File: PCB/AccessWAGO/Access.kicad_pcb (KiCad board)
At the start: 2 copper layers, 70 x 70 mm, 82 parts, among them J1 USB-C, J2 NFC, J3 I/O, J4 TC2030-USB-NL-DS, J5 NFC, J6 GND, J7 12V, J8 DOOR, J9 I/O, Q2 PMF250XNEX, SW1 ESE13V01A, U1 MD8942, U10 ESP32-S3-MINI-1, U2 MD8942, U8 G3VM-41GR8

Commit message: Silkscreen, and 21
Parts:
- added J10: Reset, RevK:AA-Pad, B.Cu at (100.0, 100.0)
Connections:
- U10 pad 25: unconnected-(U10-GPIO21-Pad25) -> Net-(J10-Pin_2)
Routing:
- net Net-(J10-Pin_2): track 0.00 -> 10.5 mm, vias 0 -> 1
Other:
- board text added: "QRQR"
- board text added: "Relay"
- board text added: "®"
- board text removed: "Relay1"

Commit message: Tweak
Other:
- copper layers 2 -> 4
- board text removed: "QRQR"

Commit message: Render
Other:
- copper layers 4 -> 2
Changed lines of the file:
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@@
 		(0 "F.Cu" signal)
 		(2 "B.Cu" signal)
-		(9 "F.Adhes" user)
-		(11 "B.Adhes" user)
+		(9 "F.Adhes" user "F.Adhesive")
+		(11 "B.Adhes" user "B.Adhesive")
 		(13 "F.Paste" user)
 		(15 "B.Paste" user)
-		(5 "F.SilkS" user)
-		(7 "B.SilkS" user)
+		(5 "F.SilkS" user "F.Silkscreen")
+		(7 "B.SilkS" user "B.Silkscreen")
 		(1 "F.Mask" user)
 		(3 "B.Mask" user)
-		(17 "Dwgs.User" user)
-		(19 "Cmts.User" user)
-		(21 "Eco1.User" user)
-		(23 "Eco2.User" user)
+		(17 "Dwgs.User" user "User.Drawings")
+		(19 "Cmts.User" user "User.Comments")
+		(21 "Eco1.User" user "User.Eco1")
+		(23 "Eco2.User" user "User.Eco2")
 		(25 "Edge.Cuts" user)
 		(27 "Margin" user)
-		(31 "F.CrtYd" user)
-		(29 "B.CrtYd" user)
+		(31 "F.CrtYd" user "F.Courtyard")
+		(29 "B.CrtYd" user "B.Courtyard")
 		(35 "F.Fab" user)
 		(33 "B.Fab" user)
-		(39 "User.1" signal)
-		(41 "User.2" signal)
+		(39 "User.1" auxiliary)
+		(41 "User.2" auxiliary "Board outline")
 	)
 	(setup
@@
 	)
 	(gr_arc
-		(start 90.3 108.7)
-		(mid 90.592893 107.992893)
-		(end 91.3 107.7)
-		(stroke
-			(width 0.05)
-			(type default)
-		)
-		(layer "Edge.Cuts")
-	)
-	(gr_arc
-		(start 73.5 108.2)
-		(mid 72.792893 107.907107)
-		(end 72.5 107.2)
+		(start 73.5 108)
+		(mid 72.792893 107.707107)
+		(end 72.5 107)
 		(stroke
 			(width 0.05)
@@
 	)
 	(gr_line
-		(start 72.5 107.2)
+		(start 72.5 107)
 		(end 72.5 77.5)
 		(stroke
@@
 	)
 	(gr_arc
-		(start 132.5 107)
-		(mid 132.207107 107.707107)
-		(end 131.5 108)
+		(start 90.3 108)
+		(mid 90.387868 107.787868)
+		(end 90.6 107.7)
 		(stroke
 			(width 0.05)
@@
 	)
 	(gr_arc
-		(start 108.7 107.7)
-		(mid 109.407107 107.992893)
-		(end 109.7 108.7)
+		(start 109.4 107.7)
+		(mid 109.612132 107.787868)
+		(end 109.7 108)
 		(stroke
 			(width 0.05)
@@
 	)
 	(gr_arc
-		(start 73.5 108.2)
-		(mid 74.5 109.2)
-		(end 73.5 110.2)
+		(start 132.5 107)
+		(mid 132.207107 107.707107)
+		(end 131.5 108)
+		(stroke
+			(width 0.05)
+			(type default)
+		)
+		(layer "Edge.Cuts")
+	)
+	(gr_arc
+		(start 73.5 108)
+		(mid 74.5 109)
+		(end 73.5 110)
 		(stroke
 			(width 0.05)
@@
 	)
 	(gr_line
-		(start 109.7 108.7)
+		(start 109.7 108)
 		(end 109.7 113)
 		(stroke
@@
 	(gr_line
 		(start 70.5 77.5)
-		(end 70.5 107.2)
+		(end 70.5 107)
 		(stroke
 			(width 0.05)
@@
 	)
 	(gr_line
-		(start 91.3 107.7)
-		(end 108.7 107.7)
+		(start 90.6 107.7)
+		(end 109.4 107.7)
 		(stroke
 			(width 0.05)
@@
 	)
 	(gr_line
-		(start 90.3 108.7)
+		(start 90.3 108)
 		(end 90.3 113)
 		(stroke
@@
 	)
 	(gr_arc
-		(start 73.5 110.2)
-		(mid 71.37868 109.32132)
-		(end 70.5 107.2)
+		(start 73.5 110)
+		(mid 71.37868 109.12132)
+		(end 70.5 107)
 		(stroke
 			(width 0.05)
@@
 		(layer "Edge.Cuts")
 	)
+	(gr_arc
+		(start 109.4 107.7)
+		(mid 109.612132 107.787868)
+		(end 109.7 108)
+		(stroke
+			(width 0.05)
+			(type default)
+		)
+		(layer "User.2")
+	)
+	(gr_line
+		(start 131.5 108)
+		(end 109.7 108)
+		(stroke
+			(width 0.05)
+			(type default)
+		)
+		(layer "User.2")
+	)
+	(gr_arc
+		(start 132.5 107)
+		(mid 132.207107 107.707107)
+		(end 131.5 108)
+		(stroke
+			(width 0.05)
+			(type default)
+		)
+		(layer "User.2")
+	)
+	(gr_arc
+		(start 90.3 108)
+		(mid 90.387868 107.787868)
+		(end 90.6 107.7)
+		(stroke
+			(width 0.05)
+			(type default)
+		)
+		(layer "User.2")
+	)
 	(gr_line
-		(start 72.5 83.8)
-		(end 72.5 108.2)
+		(start 90.6 107.7)
+		(end 109.4 107.7)
 		(stroke
-			(width 0.1)
+			(width 0.05)
 			(type default)
 		)
@@
 	)
 	(gr_line
-		(start 121.8 83.8)
-		(end 72.5 83.8)
+		(start 90.3 108)
+		(end 73.5 108)
 		(stroke
-			(width 0.1)
+			(width 0.05)
 			(type default)
 		)
@@
 	)
 	(gr_line
-		(start 121.8 108.2)
-		(end 121.8 83.8)
+		(start 132.5 77.5)
+		(end 72.5 77.5)
 		(stroke
-			(width 0.1)
+			(width 0.05)
+			(type default)
+		)
+		(layer "User.2")
+	)
+	(gr_arc
+		(start 73.5 108)
+		(mid 72.792893 107.707107)
+		(end 72.5 107)
+		(stroke
+			(width 0.05)
+			(type default)
+		)
+		(layer "User.2")
+	)
+	(gr_line
+		(start 72.5 107)
+		(end 72.5 77.5)
+		(stroke
+			(width 0.05)
 			(type default)
 		)
@@
 	)
 	(gr_line
-		(start 72.5 108.2)
-		(end 121.8 108.2)
+		(start 132.5 77.5)
+		(end 132.5 107)
 		(stroke
-			(width 0.1)
+			(width 0.05)
 			(type default)
 		)

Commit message: Tidy
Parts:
- moved C28 0.10 mm to (88.4, 106.3)
- moved J2 0.10 mm to (124.5, 95.9)
- moved J3 0.10 mm to (90.6, 85.5)
- moved J4 0.10 mm to (97.1, 89.2)
- moved J6 0.10 mm to (125.6, 85.5)
- moved J7 0.10 mm to (112.6, 85.5)
- moved J8 0.10 mm to (101.6, 85.5)
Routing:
- net GND: track 14.3 -> 21.9 mm, vias 50 -> 52
- net +3.3V: track 130.2 -> 131.2 mm
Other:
- board text removed: "15"
- board text removed: "16"
- board text removed: "17"
- board text removed: "18"
- board text removed: "19"
- board text removed: "22"
- board text removed: "23"

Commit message: Tidy
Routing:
- net +3.3V: track 131.2 -> 129.0 mm
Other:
- board text added: "TC2030"

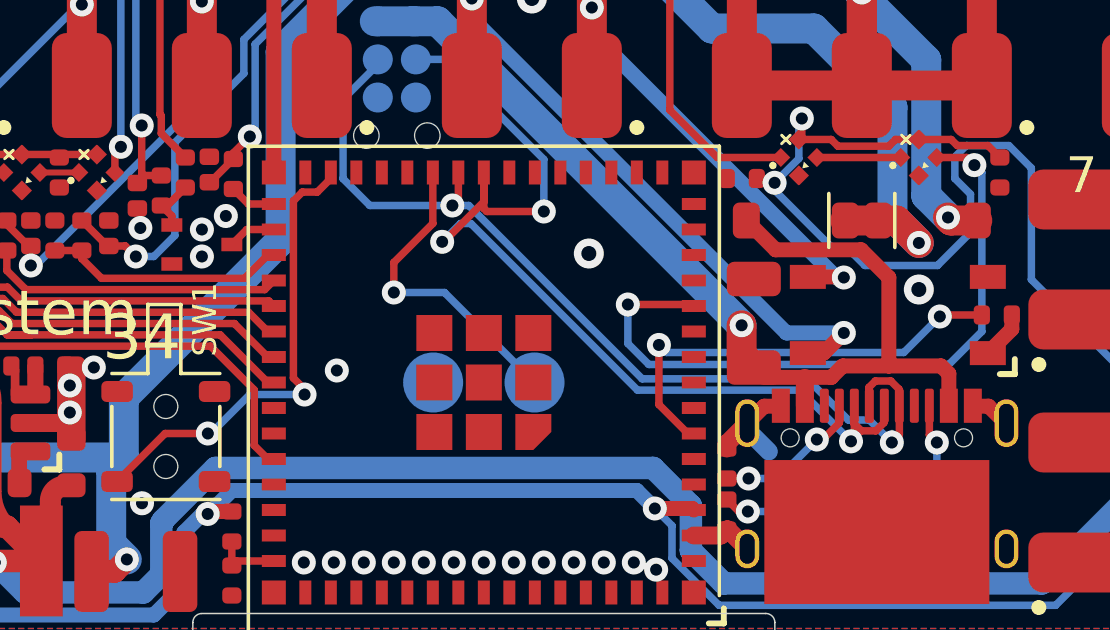
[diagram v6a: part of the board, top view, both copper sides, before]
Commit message: Component fix
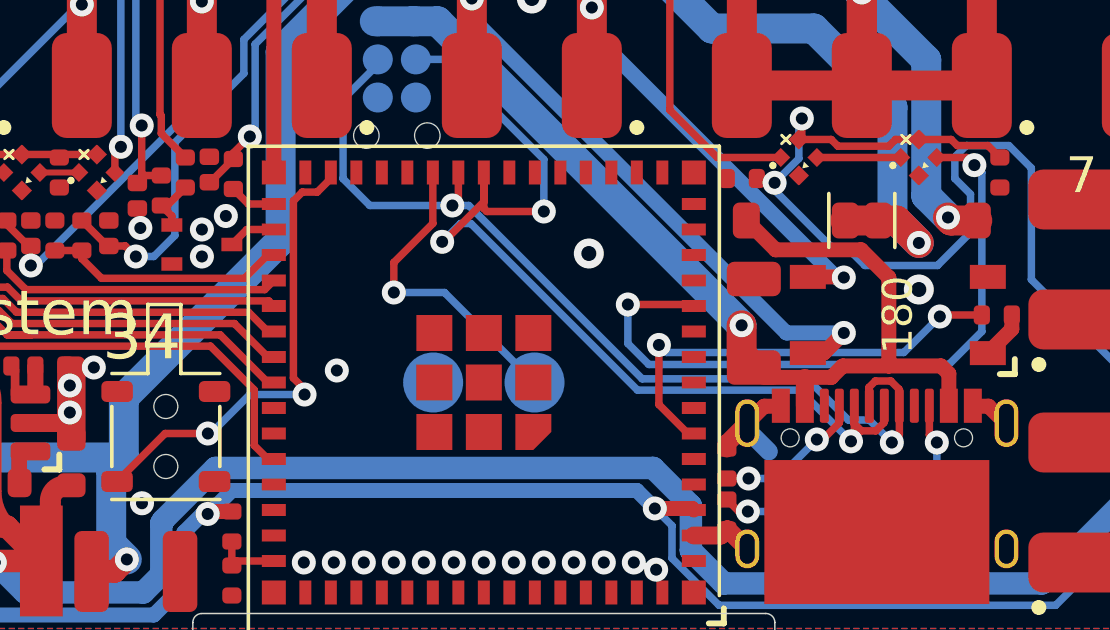
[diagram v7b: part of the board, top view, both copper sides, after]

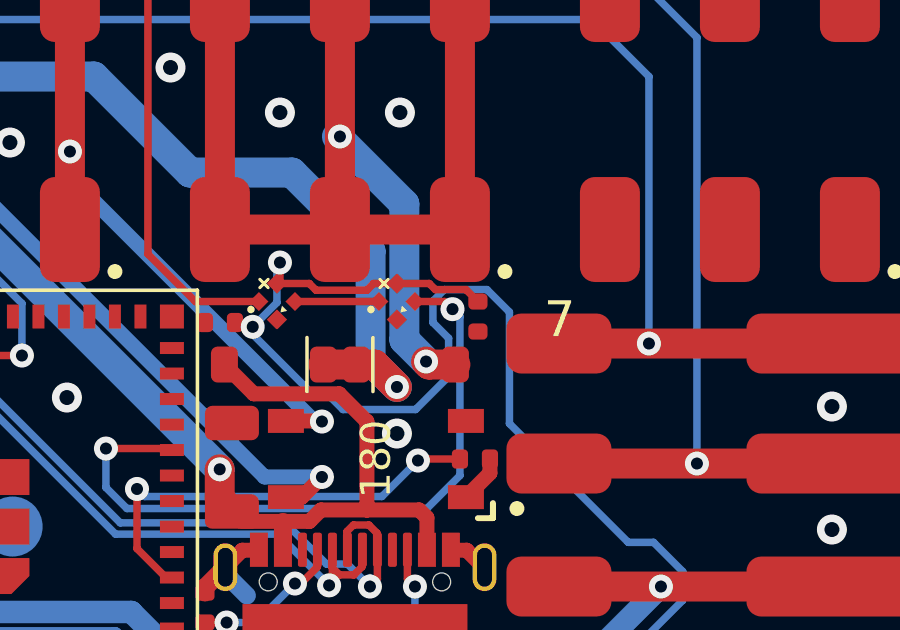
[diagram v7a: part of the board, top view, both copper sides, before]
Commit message: Bell WAGO and other updates and renders
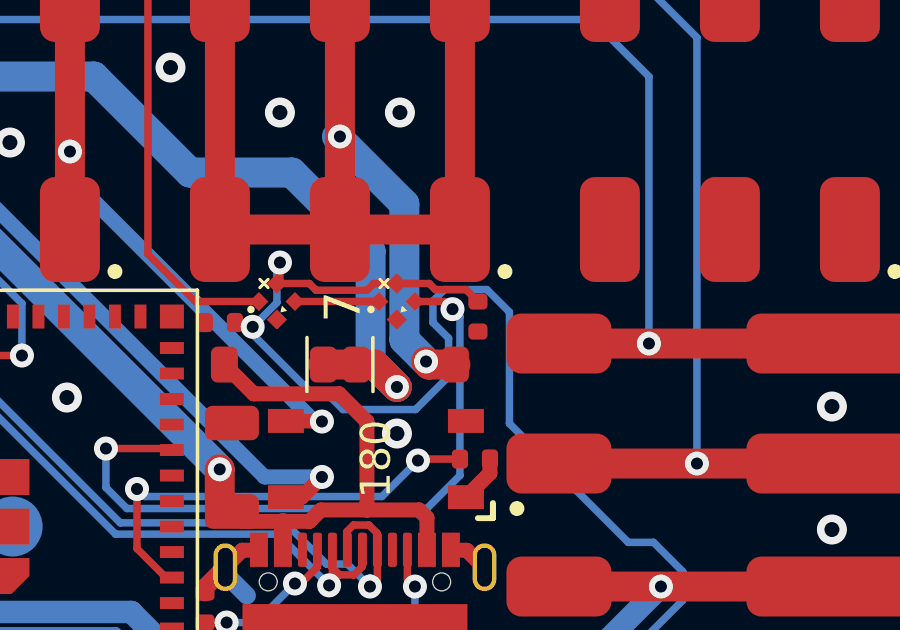
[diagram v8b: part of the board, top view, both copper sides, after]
